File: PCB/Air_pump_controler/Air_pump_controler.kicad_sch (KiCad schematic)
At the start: 21 parts, among them J1 Conn_01x03_Pin, J2 USB IN, J3 Cable mount, J4 Motor_conn, Q1 AP30N03DF, U1 CH32V003F4U6

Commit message: Update
PCB shematic and layout done rev.:0.1
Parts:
- removed C2: 4.7uF, Capacitor_SMD:C_0603_1608Metric, symbol Device:C_Small
- removed J3: Cable mount, Connector_PinHeader_2.54mm:PinHeader_1x02_P2.54mm_Vertical, symbol Connector:Conn_01x02_Pin
- added C5: 4.7uF, Capacitor_SMD:C_0402_1005Metric, symbol Device:C_Small
- added C6: TBD, Capacitor_SMD:C_0603_1608Metric, symbol Device:C_Small
- added D1: 1N4148W, Diode_SMD:D_SOD-123, symbol Diode:1N4148W
- added D2: PWR, LED_SMD:LED_0603_1608Metric, symbol Device:LED
- added R8: TBD, Resistor_SMD:R_0603_1608Metric, symbol Device:R_Small
- added R9: 100, Resistor_SMD:R_0603_1608Metric, symbol Device:R_Small
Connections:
- net +5V: now also C5.1
- net AN_POT: now also U1.3 (PA2)
- net AN_TEMP: now also U1.2 (PA1)
- net AN_V_IN: now also U1.20 (PD6)
- net GND: now also C5.2, D2.1 (K), R8.2
- net LS_SW: now also U1.16 (PD2)
- net SWIO: now also U1.15 (PD1)
- net LED: now reaches U1.11 (PC4)
- net LED: now also R9.2
- net at J4.1 (Pin_1), Q1.3 (D): now also C6.1, D1.2 (A)
- net at C3.1, C4.1, J4.2 (Pin_2)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: now also D1.1 (K)
- new net: C6.2, R8.1
- new net: D2.2 (A), R9.1
- no-connect marks 2 -> 0
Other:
- note added: "LED indicator"
- moved on the sheet: Q1, R5, R7

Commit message: Finished PCB
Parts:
- added TP1: U_RX, TestPoint:TestPoint_Pad_D1.0mm, symbol Connector:TestPoint
- added TP2: U_TX, TestPoint:TestPoint_Pad_D1.0mm, symbol Connector:TestPoint
- R4, R6: value 10k -> 100k
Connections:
- net AN_V_IN: now also U1.11 (PC4); no longer U1.20 (PD6)
- net LED: now also U1.10 (PC3); no longer U1.11 (PC4)
- net at U1.19 (PD5): now also TP2.1
- new net: TP1.1, U1.20 (PD6)
- no-connect marks 0 -> 10
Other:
- moved on the sheet: C5

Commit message: Update
software
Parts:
- R6: value 100k -> 10k
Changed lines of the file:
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@@
 			)
 		)
-		(property "Value" "100k"
-			(at 111.76 111.252 0)
+		(property "Value" "10k"
+			(at 110.998 111.252 0)
 			(effects
 				(font

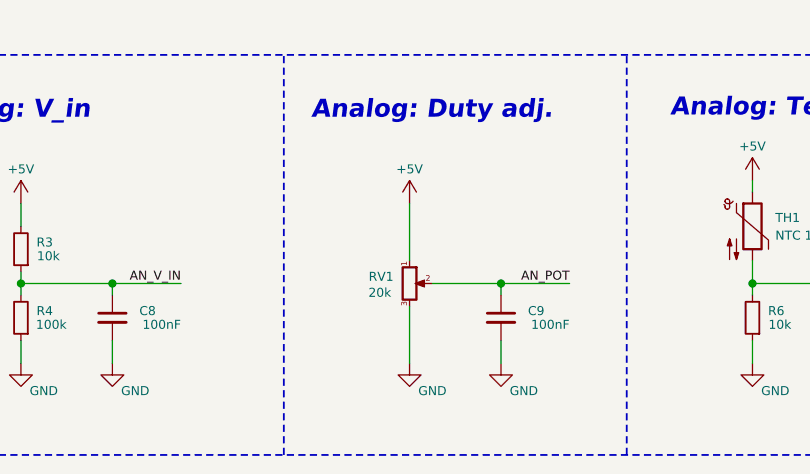
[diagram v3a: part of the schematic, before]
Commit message: Update
modified potenciometer to voltage divider
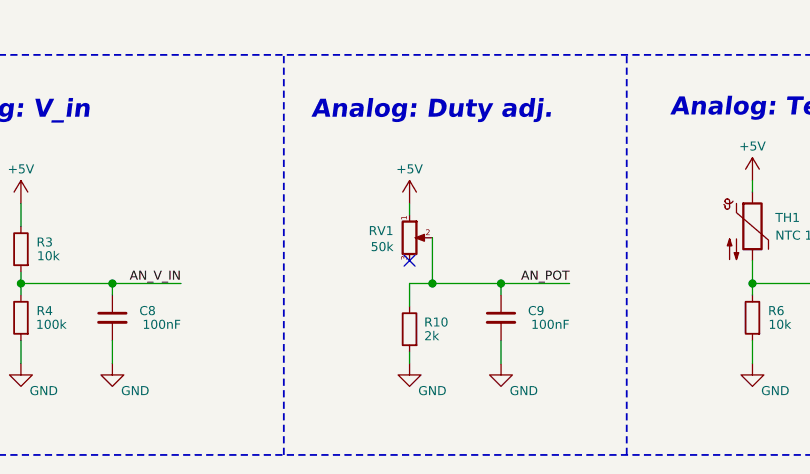
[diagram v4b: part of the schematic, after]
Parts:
- added R10: 2k, Resistor_SMD:R_0603_1608Metric, symbol Device:R_Small
- RV1: value 20k -> 50k
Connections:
- net AN_POT: now also R10.2
- net GND: now also R10.1; no longer RV1.3
- no-connect marks 10 -> 11
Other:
- moved on the sheet: RV1
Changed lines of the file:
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@@
 	)
 	(junction
+		(at 71.12 106.68)
+		(diameter 0)
+		(color 0 0 0 0)
+	)
+	(junction
 		(at 80.01 41.91)
 		(diameter 0)
@@
 		(at 213.36 39.37)
 	)
+	(no_connect
+		(at 68.58 104.14)
+	)
 	(wire
 		(pts
@@
 	(wire
 		(pts
+			(xy 71.12 106.68) (xy 68.58 106.68)
+		)
+		(stroke
+			(width 0)
+			(type default)
+		)
+	)
+	(wire
+		(pts
 			(xy 73.66 41.91) (xy 69.85 41.91)
 		)
@@
 	(wire
 		(pts
+			(xy 68.58 114.3) (xy 68.58 115.57)
+		)
+		(stroke
+			(width 0)
+			(type default)
+		)
+	)
+	(wire
+		(pts
 			(xy 63.5 45.72) (xy 63.5 41.91)
 		)
@@
 	(wire
 		(pts
+			(xy 68.58 106.68) (xy 68.58 109.22)
+		)
+		(stroke
+			(width 0)
+			(type default)
+		)
+	)
+	(wire
+		(pts
 			(xy 163.83 66.04) (xy 172.72 66.04)
 		)
@@
 	(wire
 		(pts
-			(xy 106.68 106.68) (xy 106.68 107.95)
+			(xy 71.12 101.6) (xy 71.12 106.68)
 		)
 		(stroke
@@
 	(wire
 		(pts
-			(xy 68.58 104.14) (xy 68.58 97.79)
+			(xy 106.68 106.68) (xy 106.68 107.95)
 		)
 		(stroke
@@
 	(wire
 		(pts
-			(xy 114.3 54.61) (xy 114.3 55.88)
+			(xy 68.58 99.06) (xy 68.58 97.79)
 		)
 		(stroke
@@
 	(wire
 		(pts
-			(xy 114.3 60.96) (xy 114.3 62.23)
+			(xy 114.3 54.61) (xy 114.3 55.88)
 		)
 		(stroke
@@
 	(wire
 		(pts
-			(xy 54.61 41.91) (xy 57.15 41.91)
+			(xy 114.3 60.96) (xy 114.3 62.23)
 		)
 		(stroke
@@
 	(wire
 		(pts
-			(xy 163.83 36.83) (xy 163.83 39.37)
+			(xy 54.61 41.91) (xy 57.15 41.91)
 		)
 		(stroke
@@
 	(wire
 		(pts
-			(xy 92.71 54.61) (xy 96.52 54.61)
+			(xy 163.83 36.83) (xy 163.83 39.37)
 		)
 		(stroke
@@
 	(wire
 		(pts
-			(xy 107.95 41.91) (xy 107.95 48.26)
+			(xy 92.71 54.61) (xy 96.52 54.61)
 		)
 		(stroke
@@
 	(wire
 		(pts
-			(xy 163.83 68.58) (xy 166.37 68.58)
+			(xy 107.95 41.91) (xy 107.95 48.26)
 		)
 		(stroke
@@
 	(wire
 		(pts
-			(xy 203.2 31.75) (xy 203.2 34.29)
+			(xy 163.83 68.58) (xy 166.37 68.58)
 		)
 		(stroke
@@
 	(wire
 		(pts
-			(xy 107.95 59.69) (xy 107.95 62.23)
+			(xy 203.2 31.75) (xy 203.2 34.29)
 		)
 		(stroke
@@
 	(wire
 		(pts
-			(xy 68.58 109.22) (xy 68.58 115.57)
+			(xy 107.95 59.69) (xy 107.95 62.23)
 		)
 		(stroke
@@
 	(symbol
 		(lib_id "Device:R_Potentiometer_Small")
-		(at 68.58 106.68 0)
+		(at 68.58 101.6 0)
 		(unit 1)
 		(exclude_from_sim no)
@@
 		(dnp no)
 		(property "Reference" "RV1"
-			(at 66.802 105.918 0)
+			(at 66.802 100.838 0)
 			(effects
 				(font
@@
 			)
 		)
-		(property "Value" "20k"
-			(at 66.548 107.696 0)
+		(property "Value" "50k"
+			(at 66.802 102.616 0)
 			(effects
 				(font
@@
 		)
 		(property "Footprint" "Potentiometer_SMD:Potentiometer_Bourns_TC33X_Vertical"
-			(at 68.58 106.68 0)
+			(at 68.58 101.6 0)
 			(effects
 				(font
@@
 		)
 		(property "Datasheet" "~"
-			(at 68.58 106.68 0)
+			(at 68.58 101.6 0)
 			(effects
 				(font
@@
 		)
 		(property "Description" "Potentiometer"
-			(at 68.58 106.68 0)
+			(at 68.58 101.6 0)
 			(effects
 				(font
@@
 					(unit 1)
 				)
+			)
+		)
+	)
+	(symbol
+		(lib_id "Device:R_Small")
+		(at 68.58 111.76 180)
+		(unit 1)
+		(exclude_from_sim no)
+		(in_bom yes)
+		(on_board yes)
+		(dnp no)
+		(property "Reference" "R10"
+			(at 72.898 110.998 0)
+			(effects
+				(font
+					(size 1 1)
+				)
+				(justify left)
+			)
+		)
+		(property "Value" "2k"
+			(at 71.882 112.522 0)
+			(effects
+				(font
+					(size 1 1)
+				)
+				(justify left)
+			)
+		)
+		(property "Footprint" "Resistor_SMD:R_0603_1608Metric"
+			(at 68.58 111.76 0)
+			(effects
+				(font
+					(size 1.27 1.27)
+				)
+				(hide yes)
+			)
+		)
+		(property "Datasheet" "~"
+			(at 68.58 111.76 0)
+			(effects
+				(font
+					(size 1.27 1.27)
+				)
+				(hide yes)
+			)
+		)
+		(property "Description" ""
+			(at 68.58 111.76 0)
+			(effects
+				(font
+					(size 1.27 1.27)
+				)
+				(hide yes)
+			)
+		)
+		(pin "1"
+		)
+		(pin "2"
+		)
+		(instances
+			(project "Air_pump_controler"
+				(path "/3c68f82e-901f-404a-869f-4b45aa33f8e4"
+					(reference "R10")
+					(unit 1)
+				)
